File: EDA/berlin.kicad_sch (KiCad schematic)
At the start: 615 parts, among them SW1,1 Rotary_Encoder_Switch_Chassis, SW1,10 MXSwitch, SW1,11 MXSwitch, SW1,12 MXSwitch, SW1,13 MXSwitch, SW1,14 MXSwitch, SW1,15 MXSwitch, SW1,16 Rotary_Encoder_Switch_Chassis, SW1,2 MXSwitch, SW1,3 MXSwitch, SW1,4 MXSwitch, SW1,5 MXSwitch, SW1,6 MXSwitch, SW1,7 MXSwitch, SW1,8 MXSwitch, SW1,9 MXSwitch, SW2,1 MXSwitch, SW2,10 MXSwitch, SW2,11 MXSwitch, SW2,12 MXSwitch, SW2,13 MXSwitch, SW2,14 MXSwitch, SW2,15 MXSwitch, SW2,16 MXSwitch, SW2,17 MXSwitch, SW2,18 MXSwitch, SW2,19 MXSwitch, SW2,2 MXSwitch, SW2,3 MXSwitch, SW2,4 MXSwitch, SW2,5 MXSwitch, SW2,6 MXSwitch, SW2,7 MXSwitch, SW2,9 MXSwitch, SW20-7,3 MXSwitch, SW3,1 MXSwitch, SW3,10 MXSwitch, SW3,11 MXSwitch, SW3,12 MXSwitch, SW3,13 MXSwitch, SW3,14 MXSwitch, SW3,15 MXSwitch, SW3,16 MXSwitch, SW3,17 MXSwitch, SW3,18 MXSwitch, SW3,19 MXSwitch, SW3,2 MXSwitch, SW3,3 MXSwitch, SW3,4 MXSwitch, SW3,5 MXSwitch, SW3,6 MXSwitch, SW3,7 MXSwitch, SW3,8 MXSwitch, SW3,9 MXSwitch, SW39-7,6 MXSwitch, SW4,1 MXSwitch, SW4,10 MXSwitch, SW4,11 MXSwitch, SW4,12 MXSwitch, SW4,13 MXSwitch, SW4,14 MXSwitch, SW4,15 MXSwitch, SW4,16 MXSwitch, SW4,17 MXSwitch, SW4,18 MXSwitch, SW4,19 MXSwitch, SW4,2 MXSwitch, SW4,3 MXSwitch, SW4,4 MXSwitch, SW4,5 MXSwitch, SW4,6 MXSwitch, SW4,7 MXSwitch, SW4,8 MXSwitch, SW4,9 MXSwitch, SW5,1 MXSwitch, SW5,10 MXSwitch, SW5,11 MXSwitch, SW5,12 MXSwitch, SW5,13 MXSwitch, SW5,14 MXSwitch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

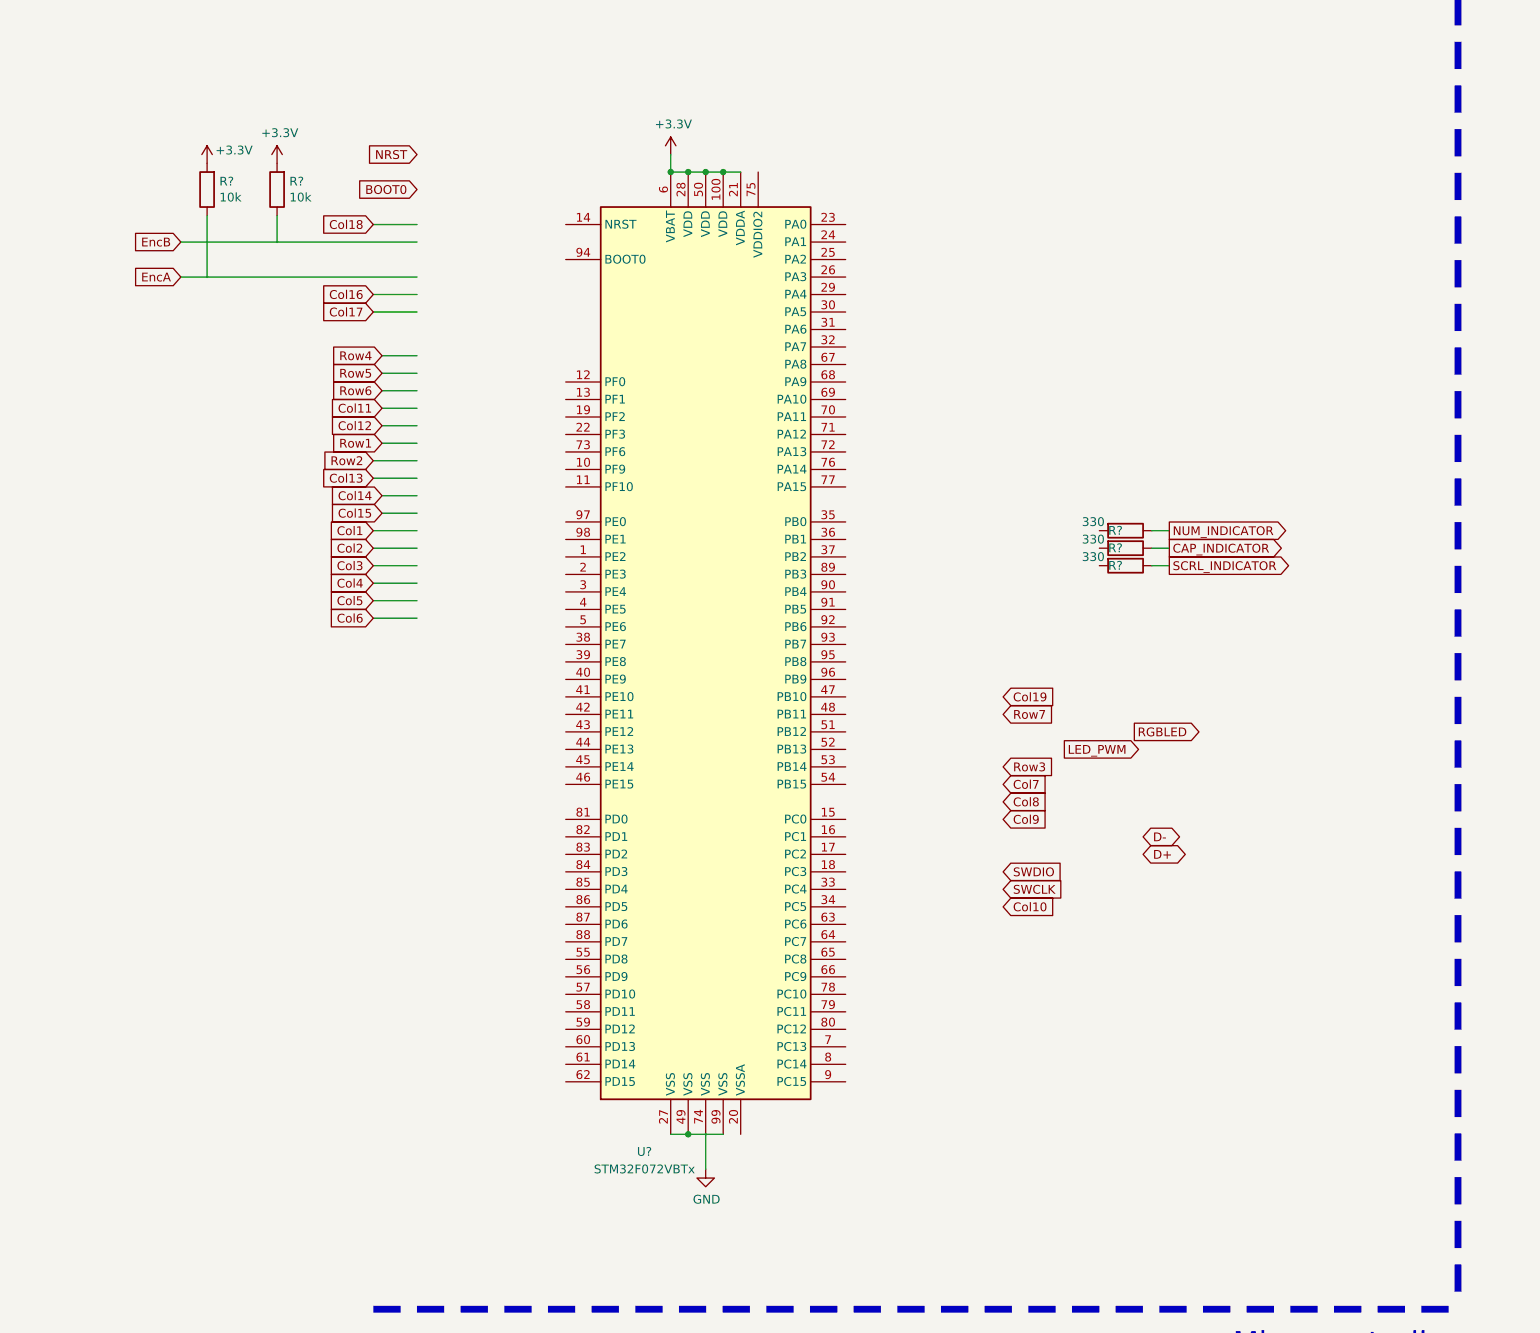
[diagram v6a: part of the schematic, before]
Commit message: initial pinout placement
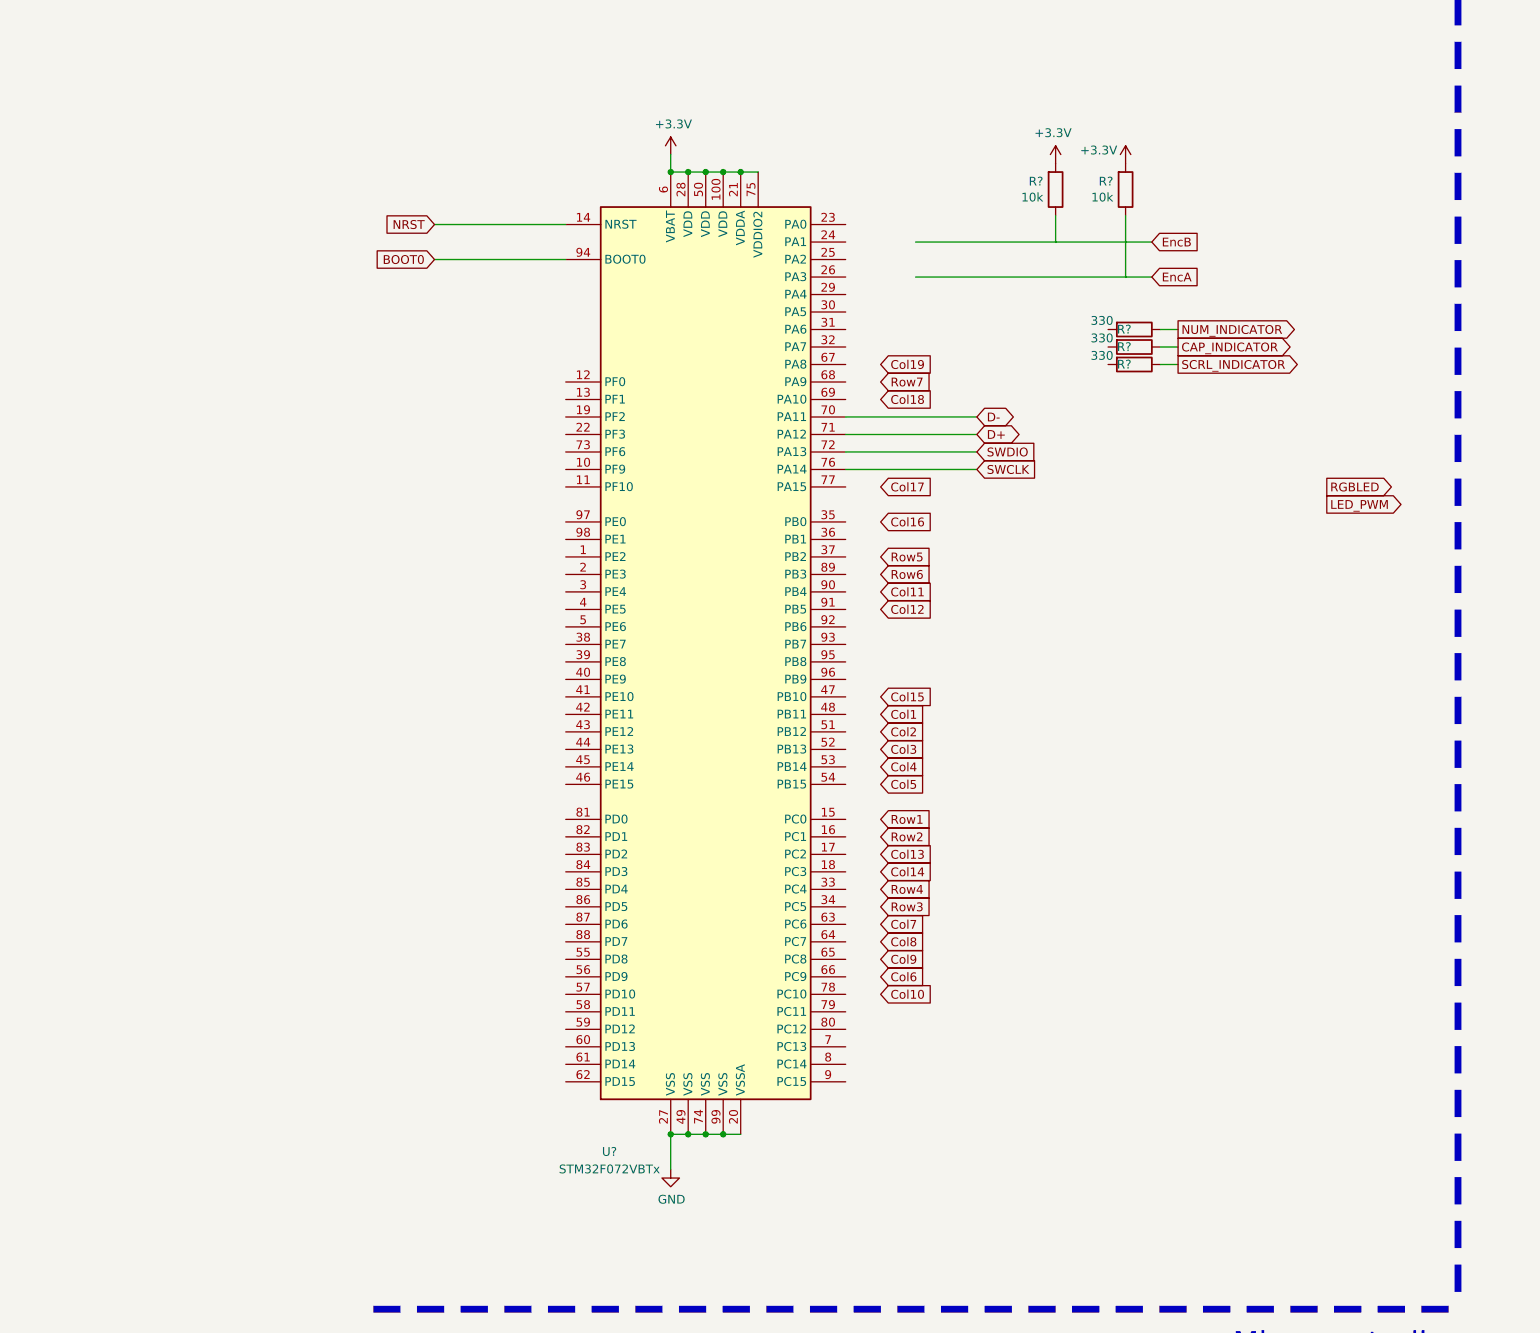
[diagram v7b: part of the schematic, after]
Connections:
- net +3V3: now also U?.75 (VDDIO2)
- net BOOT0: now also U?.94 (BOOT0)
- net D+: now also U?.71 (PA12)
- net D-: now also U?.70 (PA11)
- net GND: now also U?.20 (VSSA)
- net NRST: now also U?.14 (NRST)
- net SWCLK: now also U?.76 (PA14)
- net SWDIO: now also U?.72 (PA13)
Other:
- moved on the sheet: R?
